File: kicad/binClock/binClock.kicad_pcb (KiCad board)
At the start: 2 copper layers, 2 parts, among them U1 ESP32-C3_SUPERMINI, U2 LOGIC-74HC595N_DIP16_

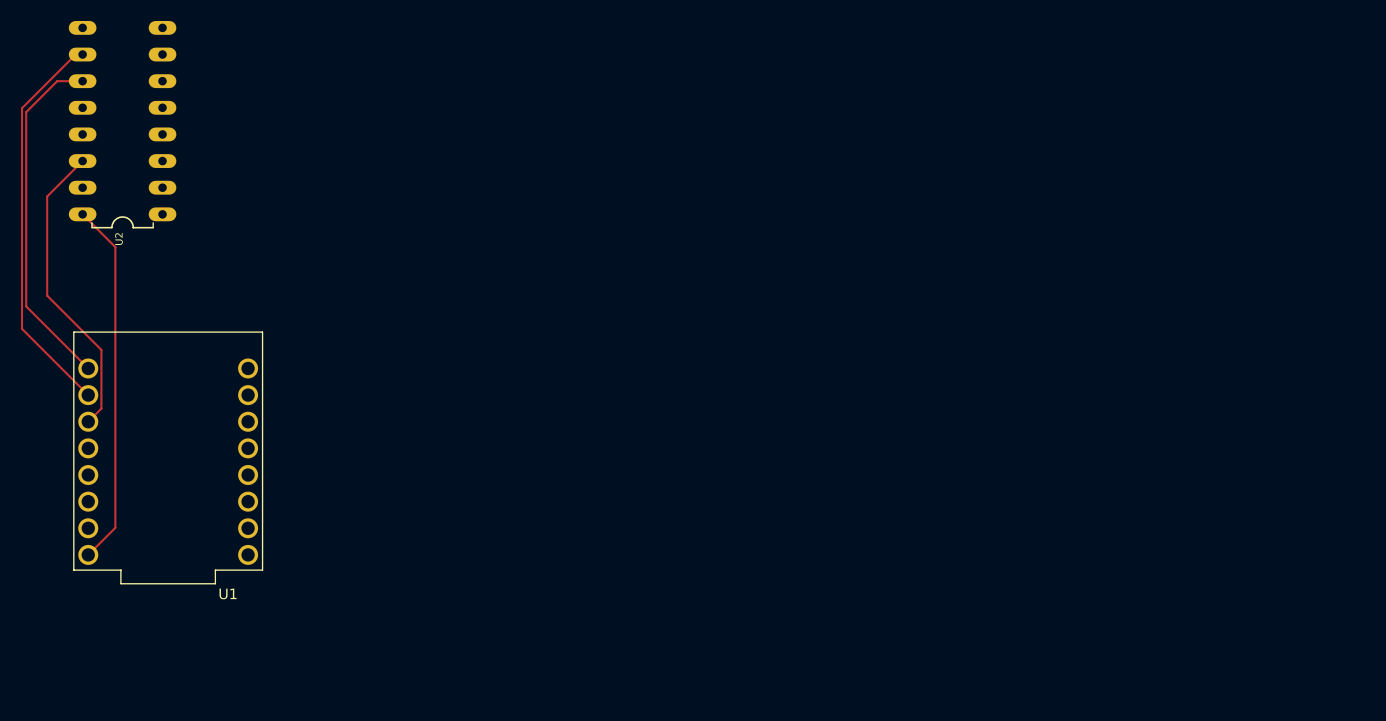
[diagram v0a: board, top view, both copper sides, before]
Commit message: Finished schematic and board layout. Included gerbers. Ordered board from jlcpcb.
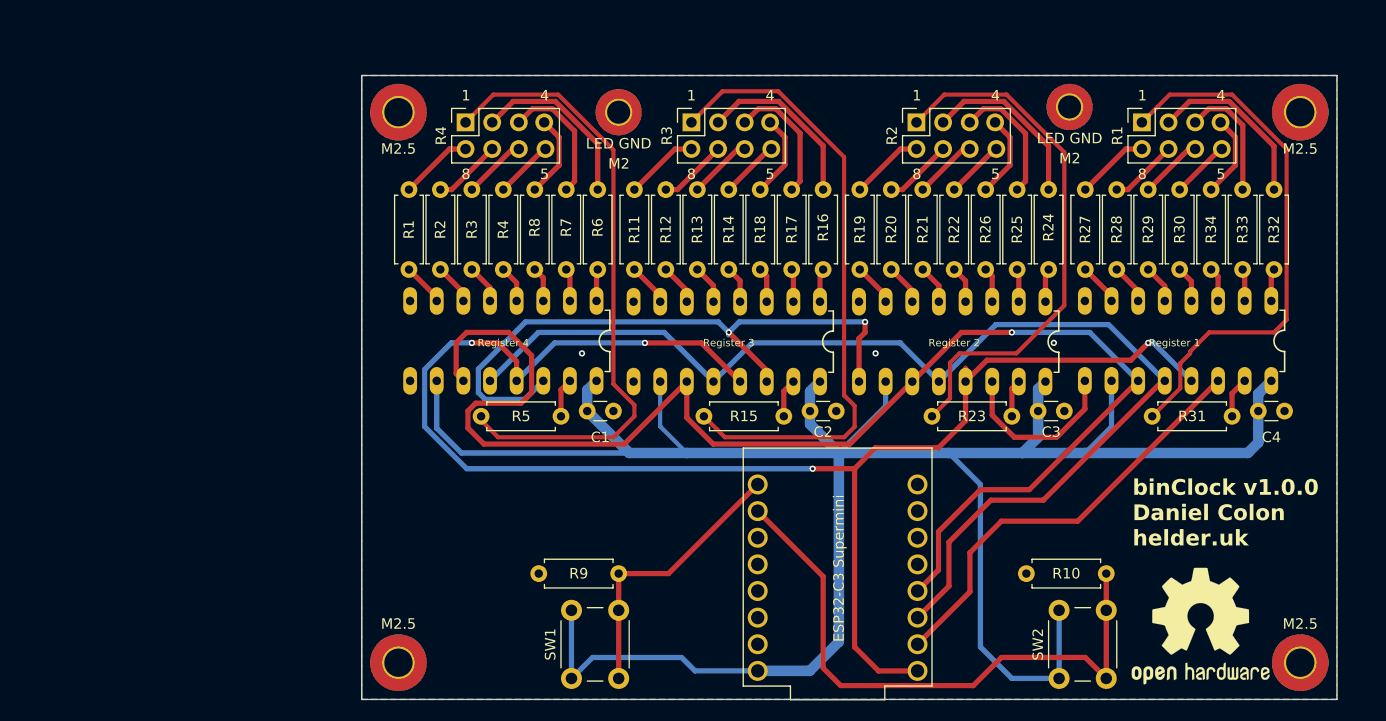
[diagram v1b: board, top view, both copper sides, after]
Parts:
- removed U1: ESP32-C3_SUPERMINI, footprints:MODULE_ESP32-C3_SUPERMINI
- removed U2: LOGIC-74HC595N_DIP16_, footprints:DIP16-2.54-20.32X5.84MM
- added C1: C_Small, Capacitor_THT:C_Disc_D3.0mm_W1.6mm_P2.50mm, F.Cu at (129.5, 112.5)
- added C2: C_Small, Capacitor_THT:C_Disc_D3.0mm_W1.6mm_P2.50mm, F.Cu at (150.8, 112.5)
- added C3: C_Small, Capacitor_THT:C_Disc_D3.0mm_W1.6mm_P2.50mm, F.Cu at (172.5, 112.5)
- added C4: C_Small, Capacitor_THT:C_Disc_D3.0mm_W1.6mm_P2.50mm, F.Cu at (193.5, 112.5)
- added ESP32-C3 Supermini: ESP32-C3_SUPERMINI, footprints:MODULE_ESP32-C3_SUPERMINI, F.Cu at (153.4, 127.4)
- added LED GND: MountingHole_LED_Tower, MountingHole:MountingHole_2.2mm_M2_Pad_TopBottom, F.Cu at (175.5, 83.5)
- added LED GND: MountingHole_LED_Tower, MountingHole:MountingHole_2.2mm_M2_Pad_TopBottom, F.Cu at (132.5, 84.0)
- added M2.5: MountingHole_Pad, MountingHole:MountingHole_2.7mm_M2.5_Pad_TopBottom, F.Cu at (197.5, 136.5)
- added M2.5: MountingHole_Pad, MountingHole:MountingHole_2.7mm_M2.5_Pad_TopBottom, F.Cu at (197.5, 84.0)
- added M2.5: MountingHole_Pad, MountingHole:MountingHole_2.7mm_M2.5_Pad_TopBottom, F.Cu at (111.5, 84.0)
- added M2.5: MountingHole_Pad, MountingHole:MountingHole_2.7mm_M2.5_Pad_TopBottom, F.Cu at (111.5, 136.5)
- added R1: R, Resistor_THT:R_Axial_DIN0207_L6.3mm_D2.5mm_P7.62mm_Horizontal, F.Cu at (112.5, 99.0)
- added R1: Conn_02x04_Clockwise, footprints:PinHeader_2x04_P2.54mm_Vertical_Clockwise, F.Cu at (182.4, 87.5)
- added R10: R, Resistor_THT:R_Axial_DIN0207_L6.3mm_D2.5mm_P7.62mm_Horizontal, F.Cu at (171.4, 128.0)
- added R11: R, Resistor_THT:R_Axial_DIN0207_L6.3mm_D2.5mm_P7.62mm_Horizontal, F.Cu at (134.0, 99.0)
- added R12: R, Resistor_THT:R_Axial_DIN0207_L6.3mm_D2.5mm_P7.62mm_Horizontal, F.Cu at (137.0, 99.0)
- added R13: R, Resistor_THT:R_Axial_DIN0207_L6.3mm_D2.5mm_P7.62mm_Horizontal, F.Cu at (140.0, 99.0)
- added R14: R, Resistor_THT:R_Axial_DIN0207_L6.3mm_D2.5mm_P7.62mm_Horizontal, F.Cu at (143.0, 99.0)
- added R15: R, Resistor_THT:R_Axial_DIN0207_L6.3mm_D2.5mm_P7.62mm_Horizontal, F.Cu at (140.6, 113.0)
- added R16: R, Resistor_THT:R_Axial_DIN0207_L6.3mm_D2.5mm_P7.62mm_Horizontal, F.Cu at (152.0, 91.4)
- added R17: R, Resistor_THT:R_Axial_DIN0207_L6.3mm_D2.5mm_P7.62mm_Horizontal, F.Cu at (149.0, 91.4)
- added R18: R, Resistor_THT:R_Axial_DIN0207_L6.3mm_D2.5mm_P7.62mm_Horizontal, F.Cu at (146.0, 91.4)
- added R19: R, Resistor_THT:R_Axial_DIN0207_L6.3mm_D2.5mm_P7.62mm_Horizontal, F.Cu at (155.5, 99.0)
- added R2: Conn_02x04_Clockwise, footprints:PinHeader_2x04_P2.54mm_Vertical_Clockwise, F.Cu at (160.9, 87.5)
- added R2: R, Resistor_THT:R_Axial_DIN0207_L6.3mm_D2.5mm_P7.62mm_Horizontal, F.Cu at (115.5, 99.0)
- added R20: R, Resistor_THT:R_Axial_DIN0207_L6.3mm_D2.5mm_P7.62mm_Horizontal, F.Cu at (158.5, 99.0)
- added R21: R, Resistor_THT:R_Axial_DIN0207_L6.3mm_D2.5mm_P7.62mm_Horizontal, F.Cu at (161.5, 99.0)
- added R22: R, Resistor_THT:R_Axial_DIN0207_L6.3mm_D2.5mm_P7.62mm_Horizontal, F.Cu at (164.5, 99.0)
- added R23: R, Resistor_THT:R_Axial_DIN0207_L6.3mm_D2.5mm_P7.62mm_Horizontal, F.Cu at (162.4, 113.0)
- added R24: R, Resistor_THT:R_Axial_DIN0207_L6.3mm_D2.5mm_P7.62mm_Horizontal, F.Cu at (173.5, 91.4)
- added R25: R, Resistor_THT:R_Axial_DIN0207_L6.3mm_D2.5mm_P7.62mm_Horizontal, F.Cu at (170.5, 91.4)
- added R26: R, Resistor_THT:R_Axial_DIN0207_L6.3mm_D2.5mm_P7.62mm_Horizontal, F.Cu at (167.5, 91.4)
- added R27: R, Resistor_THT:R_Axial_DIN0207_L6.3mm_D2.5mm_P7.62mm_Horizontal, F.Cu at (177.0, 99.0)
- added R28: R, Resistor_THT:R_Axial_DIN0207_L6.3mm_D2.5mm_P7.62mm_Horizontal, F.Cu at (180.0, 99.0)
- added R29: R, Resistor_THT:R_Axial_DIN0207_L6.3mm_D2.5mm_P7.62mm_Horizontal, F.Cu at (183.0, 99.0)
- added R3: R, Resistor_THT:R_Axial_DIN0207_L6.3mm_D2.5mm_P7.62mm_Horizontal, F.Cu at (118.5, 99.0)
- added R3: Conn_02x04_Clockwise, footprints:PinHeader_2x04_P2.54mm_Vertical_Clockwise, F.Cu at (139.4, 87.5)
- added R30: R, Resistor_THT:R_Axial_DIN0207_L6.3mm_D2.5mm_P7.62mm_Horizontal, F.Cu at (186.0, 99.0)
- added R31: R, Resistor_THT:R_Axial_DIN0207_L6.3mm_D2.5mm_P7.62mm_Horizontal, F.Cu at (183.4, 113.0)
- added R32: R, Resistor_THT:R_Axial_DIN0207_L6.3mm_D2.5mm_P7.62mm_Horizontal, F.Cu at (195.0, 91.4)
- added R33: R, Resistor_THT:R_Axial_DIN0207_L6.3mm_D2.5mm_P7.62mm_Horizontal, F.Cu at (192.0, 91.4)
- added R34: R, Resistor_THT:R_Axial_DIN0207_L6.3mm_D2.5mm_P7.62mm_Horizontal, F.Cu at (189.0, 91.4)
- added R4: Conn_02x04_Clockwise, footprints:PinHeader_2x04_P2.54mm_Vertical_Clockwise, F.Cu at (117.9, 87.5)
- added R4: R, Resistor_THT:R_Axial_DIN0207_L6.3mm_D2.5mm_P7.62mm_Horizontal, F.Cu at (121.5, 99.0)
- added R5: R, Resistor_THT:R_Axial_DIN0207_L6.3mm_D2.5mm_P7.62mm_Horizontal, F.Cu at (119.4, 113.0)
- added R6: R, Resistor_THT:R_Axial_DIN0207_L6.3mm_D2.5mm_P7.62mm_Horizontal, F.Cu at (130.5, 91.4)
- added R7: R, Resistor_THT:R_Axial_DIN0207_L6.3mm_D2.5mm_P7.62mm_Horizontal, F.Cu at (127.5, 91.4)
- added R8: R, Resistor_THT:R_Axial_DIN0207_L6.3mm_D2.5mm_P7.62mm_Horizontal, F.Cu at (124.5, 91.4)
- added R9: R, Resistor_THT:R_Axial_DIN0207_L6.3mm_D2.5mm_P7.62mm_Horizontal, F.Cu at (124.9, 128.0)
- added REF**: OSHW-Logo2_14.6x12mm_SilkScreen, Symbol:OSHW-Logo2_14.6x12mm_SilkScreen, F.Cu at (188.0, 133.0)
- added Register 1: ~, footprints:DIP16-2.54-20.32X5.84MM, F.Cu at (185.8, 105.8)
- added Register 2: ~, footprints:DIP16-2.54-20.32X5.84MM, F.Cu at (164.3, 105.9)
- added Register 3: ~, footprints:DIP16-2.54-20.32X5.84MM, F.Cu at (142.8, 105.9)
- added Register 4: ~, footprints:DIP16-2.54-20.32X5.84MM, F.Cu at (121.5, 105.8)
- added SW1: SW_Push, Button_Switch_THT:SW_PUSH_6mm, F.Cu at (128.0, 138.0)
- added SW2: SW_Push, Button_Switch_THT:SW_PUSH_6mm, F.Cu at (174.5, 138.0)
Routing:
- net +5V: track 34.8 -> 227.6 mm
- net Net-(U1-OE): track 0.00 -> 152.0 mm, vias 0 -> 4
- net Net-(U1-SCK): track 0.00 -> 133.7 mm, vias 0 -> 1
- net Net-(U1-RCK): track 0.00 -> 111.1 mm
- net Net-(U1-SER): track 0.00 -> 61.4 mm, vias 0 -> 2
- net Net-(J1-Pin_1): track 0.00 -> 60.7 mm
- net Net-(J2-Pin_1): track 0.00 -> 60.1 mm
- net Net-(U3-GPIO1/A): track 0.00 -> 57.2 mm
- net Net-(J4-Pin_1): track 0.00 -> 51.5 mm
- net Net-(J3-Pin_1): track 0.00 -> 51.1 mm
- net Net-(U3-GPIO6/MOSI): track 0.00 -> 41.3 mm
- net Net-(U1-GPIO1): track 37.9 -> 0.00 mm
- net Net-(U1-GPIO0): track 33.5 -> 0.00 mm
- net Net-(U1-GPIO2): track 28.9 -> 0.00 mm
- net Net-(U3-GPIO0/A): track 0.00 -> 26.8 mm
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- added copper zone on B.Cu, net GND
- added copper zone on F.Cu, net GND
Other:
- board outline added: 93 x 59.5 mm
- board text added: "1"
- board text added: "4"
- board text added: "5"
- board text added: "8"
- board text added: "M2"
- board text added: "binClock v1.0.0 Daniel Colon helder.uk"
